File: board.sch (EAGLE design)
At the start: 85 parts, among them J1 AVR_SPI_PRG_6NS, U1 VS1063DS, U2 USD-SOCKETNEW, U3 MAX1555, U4 TPS2112A, U6 74HC595, U7 3.3V, U8 1.8V, Y1 12.288MHz, Y2 8MHz

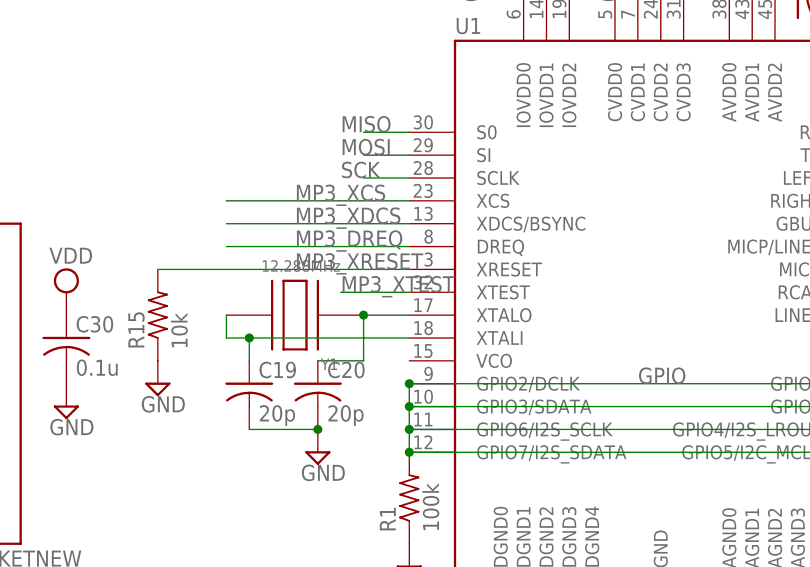
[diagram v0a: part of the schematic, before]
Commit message: Connected XTest on vs1063 to VDD
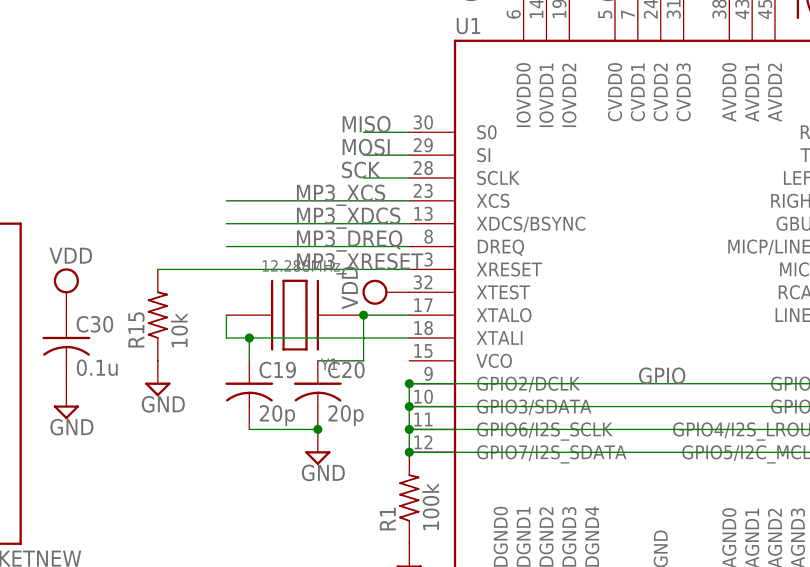
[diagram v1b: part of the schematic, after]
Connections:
- removed net MP3_XTEST: U1.XTEST
- net VDD: now also U1.XTEST
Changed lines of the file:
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@@
 <part name="SUPPLY51" library="supply2" deviceset="VDD" device=""/>
 <part name="C33" library="rcl" deviceset="C-US" device="C0603K" value="1u"/>
+<part name="SUPPLY53" library="supply2" deviceset="VDD" device=""/>
 </parts>
 <sheets>
@@
 <instance part="SUPPLY51" gate="G$1" x="2.54" y="17.78" rot="R90"/>
 <instance part="C33" gate="G$1" x="175.26" y="124.46" rot="R270"/>
+<instance part="SUPPLY53" gate="G$1" x="147.32" y="55.88" rot="R90"/>
 </instances>
 <busses>
@@
 <pinref part="SUPPLY51" gate="G$1" pin="VDD"/>
 </segment>
+<segment>
+<pinref part="U1" gate="G$1" pin="XTEST"/>
+<pinref part="SUPPLY53" gate="G$1" pin="VDD"/>
+</segment>
 </net>
 <net name="GPIO" class="0">
@@
 </segment>
 </net>
-<net name="MP3_XTEST" class="0">
-<segment>
-<pinref part="U1" gate="G$1" pin="XTEST"/>
-<wire x1="149.86" y1="55.88" x2="142.24" y2="55.88" width="0.1524" layer="91"/>
-<label x="142.24" y="55.88" size="1.778" layer="95"/>
-</segment>
-</net>

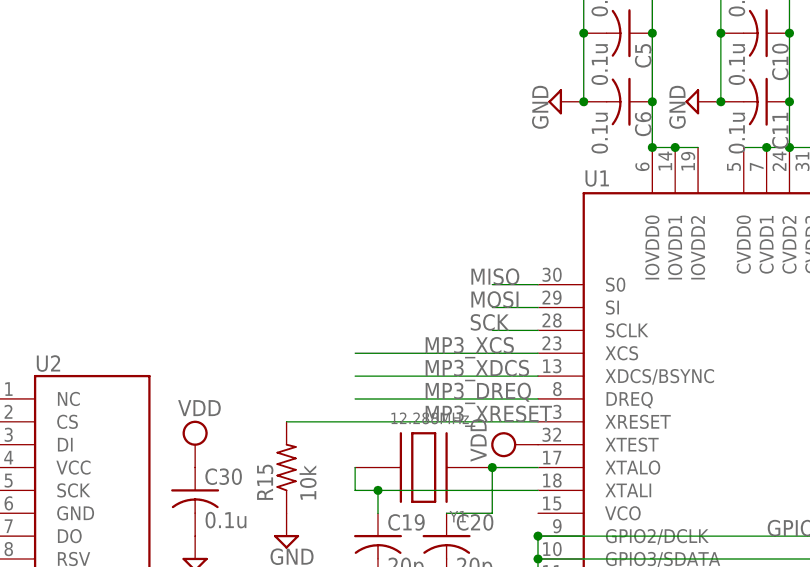
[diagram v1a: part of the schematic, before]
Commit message: Added pull-ups to mp3 cs lines
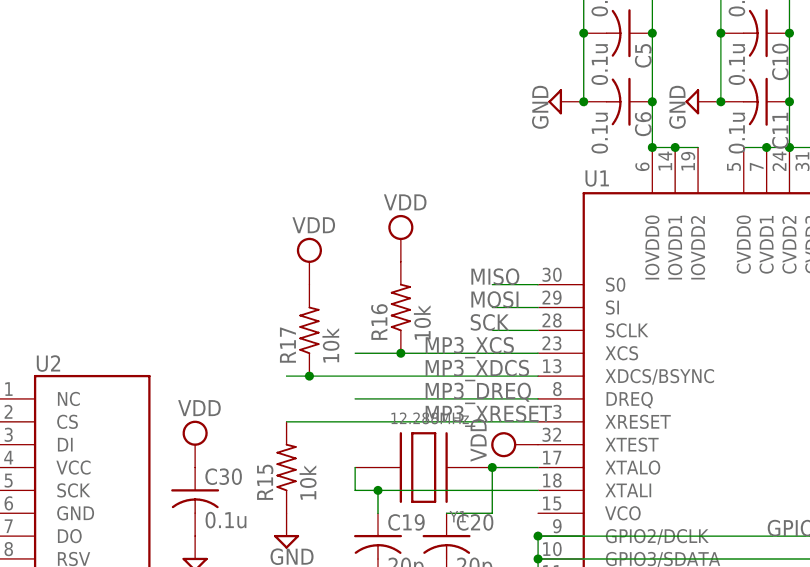
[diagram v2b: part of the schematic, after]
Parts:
- added R16, R17: 10k, rcl:R-US_R0603W
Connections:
- net MP3_XCS: now also R16.1
- net MP3_XDCS: now also R17.1
- net VDD: now also R16.2, R17.2
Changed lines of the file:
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@@
 <part name="C33" library="rcl" deviceset="C-US" device="C0603K" value="1u"/>
 <part name="SUPPLY53" library="supply2" deviceset="VDD" device=""/>
+<part name="R16" library="rcl" deviceset="R-US_" device="R0603W" value="10k"/>
+<part name="R17" library="rcl" deviceset="R-US_" device="R0603W" value="10k"/>
+<part name="SUPPLY54" library="supply2" deviceset="VDD" device=""/>
+<part name="SUPPLY55" library="supply2" deviceset="VDD" device=""/>
 </parts>
 <sheets>
@@
 <instance part="C33" gate="G$1" x="175.26" y="124.46" rot="R270"/>
 <instance part="SUPPLY53" gate="G$1" x="147.32" y="55.88" rot="R90"/>
+<instance part="R16" gate="G$1" x="134.62" y="71.12" rot="R90"/>
+<instance part="R17" gate="G$1" x="124.46" y="68.58" rot="R90"/>
+<instance part="SUPPLY54" gate="G$1" x="124.46" y="76.2"/>
+<instance part="SUPPLY55" gate="G$1" x="134.62" y="78.74"/>
 </instances>
 <busses>
@@
 <pinref part="SUPPLY53" gate="G$1" pin="VDD"/>
 </segment>
+<segment>
+<pinref part="R17" gate="G$1" pin="2"/>
+<pinref part="SUPPLY54" gate="G$1" pin="VDD"/>
+</segment>
+<segment>
+<pinref part="R16" gate="G$1" pin="2"/>
+<pinref part="SUPPLY55" gate="G$1" pin="VDD"/>
+</segment>
 </net>
 <net name="GPIO" class="0">
@@
 <segment>
 <pinref part="U1" gate="G$1" pin="XCS"/>
-<wire x1="129.54" y1="66.04" x2="149.86" y2="66.04" width="0.1524" layer="91"/>
+<wire x1="129.54" y1="66.04" x2="134.62" y2="66.04" width="0.1524" layer="91"/>
 <label x="137.16" y="66.04" size="1.778" layer="95"/>
+<pinref part="R16" gate="G$1" pin="1"/>
+<wire x1="134.62" y1="66.04" x2="149.86" y2="66.04" width="0.1524" layer="91"/>
+<junction x="134.62" y="66.04"/>
 </segment>
 <segment>
@@
 <segment>
 <pinref part="U1" gate="G$1" pin="XDCS/BSYNC"/>
-<wire x1="129.54" y1="63.5" x2="149.86" y2="63.5" width="0.1524" layer="91"/>
+<wire x1="124.46" y1="63.5" x2="149.86" y2="63.5" width="0.1524" layer="91"/>
 <label x="137.16" y="63.5" size="1.778" layer="95"/>
-</segment>
-<segment>
+<pinref part="R17" gate="G$1" pin="1"/>
+<wire x1="124.46" y1="63.5" x2="121.92" y2="63.5" width="0.1524" layer="91"/>
+<junction x="124.46" y="63.5"/>
+</segment>
+<segment>

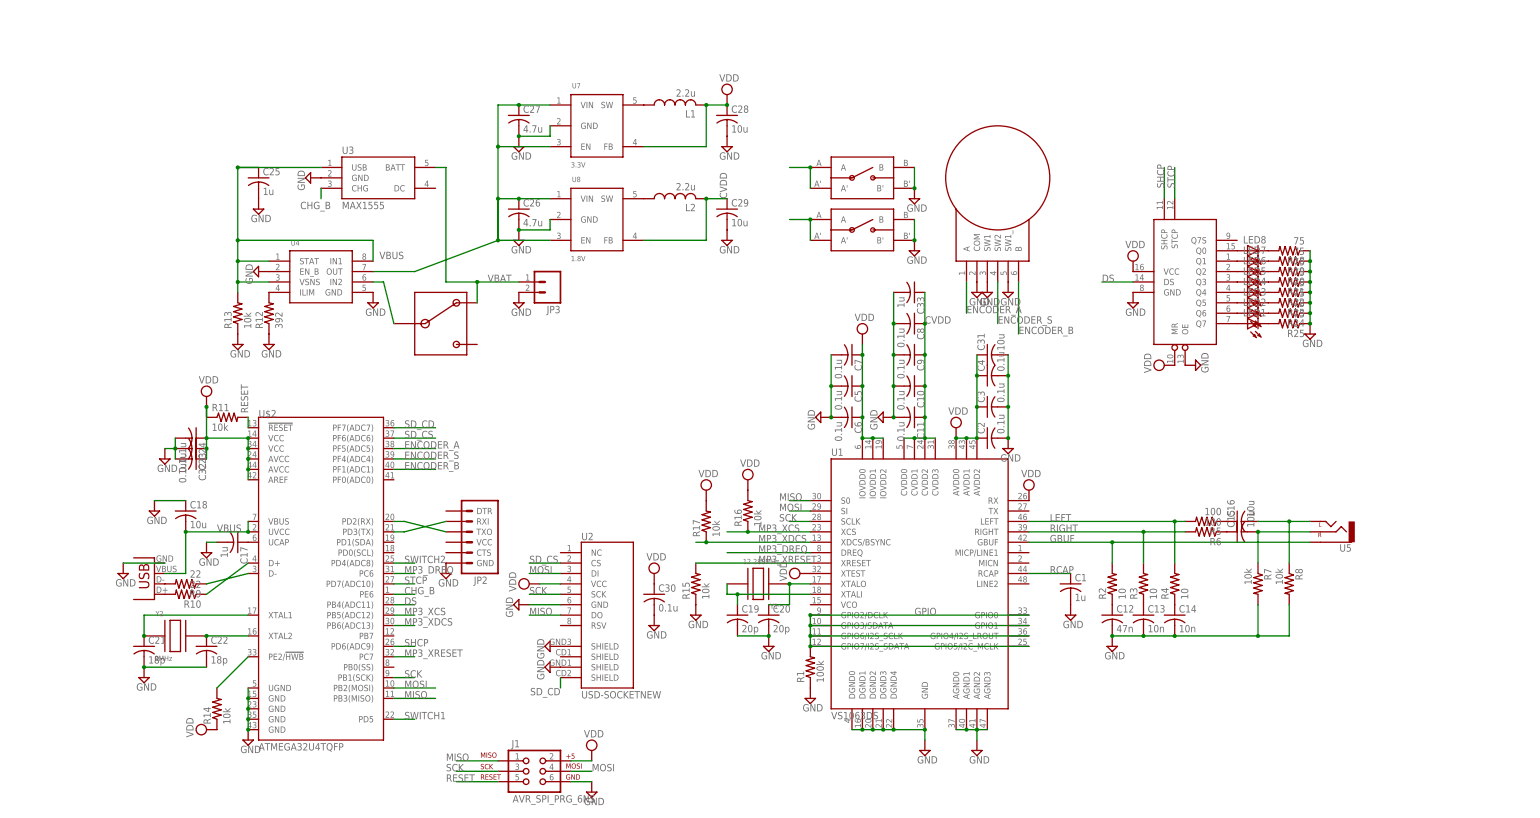
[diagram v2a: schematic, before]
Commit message: Beginning to switch to atmega32u2
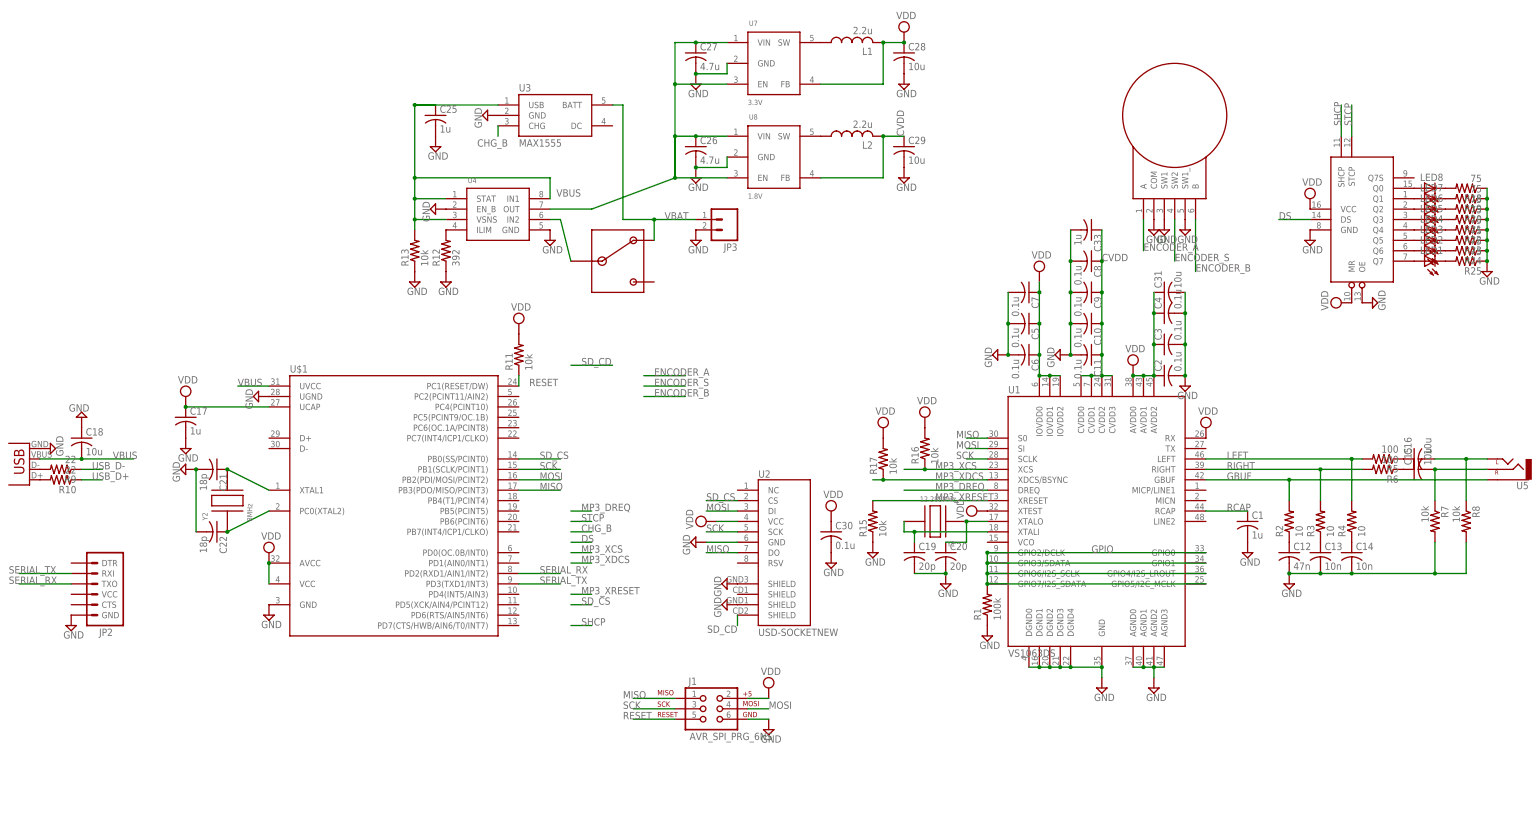
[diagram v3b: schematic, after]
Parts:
- removed C23, C24, C32: 0.1u, rcl:C-USC0603K
- removed R14: 10k, rcl:R-US_R0603
- removed S2, S3: EVQ-PSC, mkmp3:EVQ-PSC
- removed U$2: ATMEGA32U4TQFP, SparkFun-DigitalIC:ATMEGA32U4TQFP
- added U$1: ATMEGA32U2, CEDT:ATMEGA32U2
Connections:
- removed net N$15: JP2.TXO, U$2.PD2(RX)
- removed net N$16: JP2.RXI, U$2.PD3(TX)
- removed net N$38: R14.2, U$2.PE2/!HWB
- removed net N$9: C17.1, U$2.UCAP
- removed net SWITCH1: S2.A, S2.A', U$2.PD5
- removed net SWITCH2: S3.A, S3.A', U$2.PD4(ADC8)
- new net SERIAL_RX: JP2.TXO, U$1.PD2(RXD1/AIN1/INT2)
- new net SERIAL_TX: JP2.RXI, U$1.PD3(TXD1/INT3)
- net CHG_B: no longer U$2.PE6
- net DS: no longer U$2.PB4(ADC11)
- net ENCODER_A: no longer U$2.PF5(ADC5)
- net ENCODER_B: no longer U$2.PF1(ADC1)
- net ENCODER_S: no longer U$2.PF4(ADC4)
- net GND: now also U$1.GND, U$1.UGND; no longer C23.2, C24.2, C32.2, S2.B, S2.B', S3.B, S3.B', U$2.GND@15, U$2.GND@23, U$2.GND@35, U$2.GND@43, U$2.UGND
- net MISO: now also U$1.PB3(PDO/MISO/PCINT3); no longer U$2.PB3(MISO)
- net MOSI: now also U$1.PB2(PDI/MOSI/PCINT2); no longer U$2.PB2(MOSI)
- net MP3_DREQ: no longer U$2.PC6
- net MP3_XCS: no longer U$2.PB5(ADC12)
- net MP3_XDCS: no longer U$2.PB6(ADC13)
- net MP3_XRESET: no longer U$2.PC7
- net N$14: now also U$1.PC0(XTAL2), Y2.P$1; no longer U$2.XTAL2, Y2.P$2
- net N$2: now also U$1.XTAL1, Y2.P$2; no longer U$2.XTAL1, Y2.P$1
- net RESET: now also R11.1, U$1.PC1(RESET/DW); no longer R11.2, U$2.!RESET
- net SCK: now also U$1.PB1(SCLK/PCINT1); no longer U$2.PB1(SCK)
- net SD_CD: no longer U$2.PF7(ADC7)
- net SD_CS: now also U$1.PB0(SS/PCINT0); no longer U$2.PF6(ADC6)
- net SHCP: no longer U$2.PD6(ADC9)
- net STCP: no longer U$2.PD7(ADC10)
- net USB_D+: no longer U$2.D+
- net USB_D-: no longer U$2.D-
- net VBUS: now also U$1.UVCC; no longer U$2.UVCC, U$2.VBUS
- net VDD: now also C17.1, R11.2, U$1.AVCC, U$1.UCAP, U$1.VCC; no longer C23.1, C24.1, C32.1, R11.1, R14.1, U$2.AREF, U$2.AVCC@24, U$2.AVCC@44, U$2.VCC@14, U$2.VCC@34
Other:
- moved on the sheet: C1, C10, C11, C12, C13, C14, C15, C16, C17, C18, C19, C2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

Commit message: Switched to smaller uC and VS1003 chip
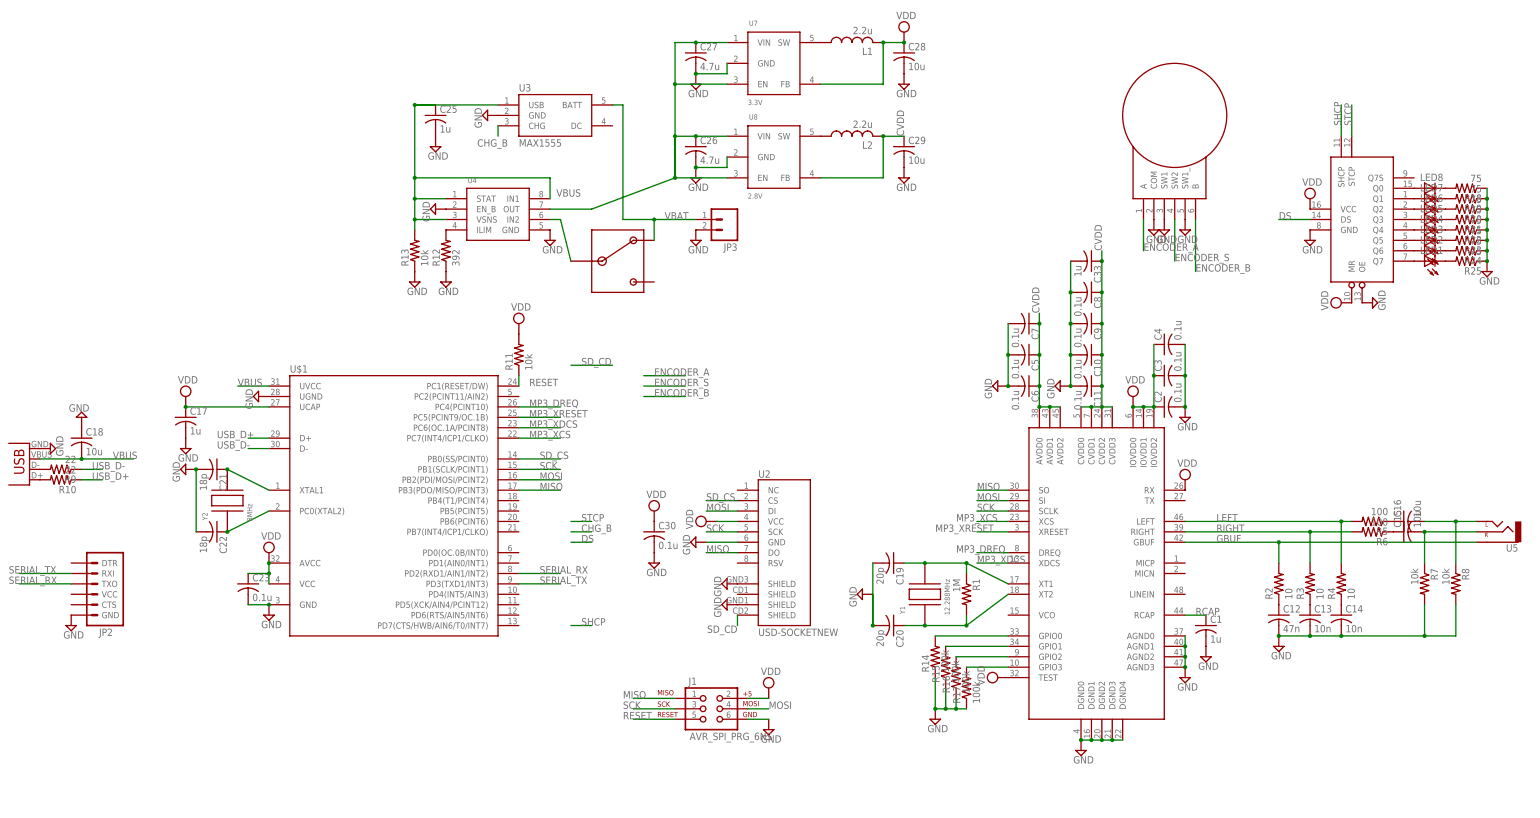
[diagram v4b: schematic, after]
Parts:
- removed C31: 10u, rcl:C-USC0603K
- removed U1: VS1063DS, mkmp3:VS1063DS
- added C23: 0.1u, rcl:C-USC0603K
- added R14: 100k, rcl:R-US_R0603W
- added U$2: VS1003, mkmp3:VS1003
- R1: value 100k -> 1M
- R15: value 10k -> 100k; device rcl:R-US_R0603W -> rcl:R-US_R0603
- R16, R17: value 10k -> 100k
- U8: value 1.8V -> 2.8V
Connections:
- removed net GPIO: R1.2, U1.GPIO0, U1.GPIO1, U1.GPIO2/DCLK, U1.GPIO3/SDATA, U1.GPIO4/I2S_LROUT, U1.GPIO5/I2C_MCLK, U1.GPIO6/I2S_SCLK, U1.GPIO7/I2S_SDATA
- new net GPIO0: R14.2, U$2.GPIO0
- new net GPIO1: R15.2, U$2.GPIO1
- new net GPIO2: R16.2, U$2.GPIO2
- new net GPIO3: R17.2, U$2.GPIO3
- net CVDD: now also C5.1, C6.1, C7.1, U$2.AVDD0, U$2.AVDD1, U$2.AVDD2, U$2.CVDD0, U$2.CVDD1, U$2.CVDD2, U$2.CVDD3; no longer U1.CVDD0, U1.CVDD1, U1.CVDD2, U1.CVDD3
- net GBUF: now also U$2.GBUF; no longer U1.GBUF
- net GND: now also C23.2, R14.1, R16.1, R17.1, U$2.AGND0, U$2.AGND1, U$2.AGND2, U$2.AGND3, U$2.DGND0, U$2.DGND1, U$2.DGND2, U$2.DGND3, U$2.DGND4; no longer C31.2, R1.1, U1.AGND0, U1.AGND1, U1.AGND2, U1.AGND3, U1.DGND0, U1.DGND1, U1.DGND2, U1.DGND3, U1.DGND4, U1.GND
- net LEFT: now also U$2.LEFT; no longer U1.LEFT
- net MISO: now also U$2.SO; no longer U1.S0
- net MOSI: now also U$2.SI; no longer U1.SI
- net MP3_DREQ: now also U$1.PC4(PCINT10), U$2.DREQ; no longer U1.DREQ
- net MP3_XCS: now also U$1.PC7(INT4/ICP1/CLKO), U$2.XCS; no longer R16.1, U1.XCS
- net MP3_XDCS: now also U$1.PC6(OC.1A/PCINT8), U$2.XDCS; no longer R17.1, U1.XDCS/BSYNC
- net MP3_XRESET: now also U$1.PC5(PCINT9/OC.1B), U$2.XRESET; no longer R15.2, U1.XRESET
- net N$7: now also R1.2, U$2.XT2; no longer U1.XTALO
- net N$8: now also R1.1, U$2.XT1; no longer U1.XTALI
- net RCAP: now also U$2.RCAP; no longer U1.RCAP
- net RIGHT: now also U$2.RIGHT; no longer U1.RIGHT
- net SCK: now also U$2.SCLK; no longer U1.SCLK
- net USB_D+: now also U$1.D+
- net USB_D-: now also U$1.D-
- net VDD: now also C23.1, U$2.IOVDD0, U$2.IOVDD1, U$2.IOVDD2, U$2.RX, U$2.TEST; no longer C31.1, C5.1, C6.1, C7.1, R16.2, R17.2, U1.AVDD0, U1.AVDD1, U1.AVDD2, U1.IOVDD0, U1.IOVDD1, U1.IOVDD2, U1.RX, U1.XTEST
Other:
- moved on the sheet: C1, C10, C11, C12, C13, C14, C15, C16, C19, C2, C20, C3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
